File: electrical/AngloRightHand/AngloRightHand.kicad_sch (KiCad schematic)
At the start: 50 parts, among them J4 TC2030-NL, U1 DRV5053VAQDBZR, U10 DRV5053VAQDBZR, U11 DRV5053VAQDBZR, U12 DRV5053VAQDBZR, U13 DRV5053VAQDBZR, U14 DRV5053VAQDBZR, U15 DRV5053VAQDBZR, U16 DRV5053VAQDBZR, U17 DRV5053VAQDBZR, U18 DRV5053VAQDBZR, U19 STM32L072CBTx, U2 CD74HC4067SM, U5 DRV5053VAQDBZR, U6 DRV5053VAQDBZR, U7 DRV5053VAQDBZR, U8 DRV5053VAQDBZR, U9 DRV5053VAQDBZR

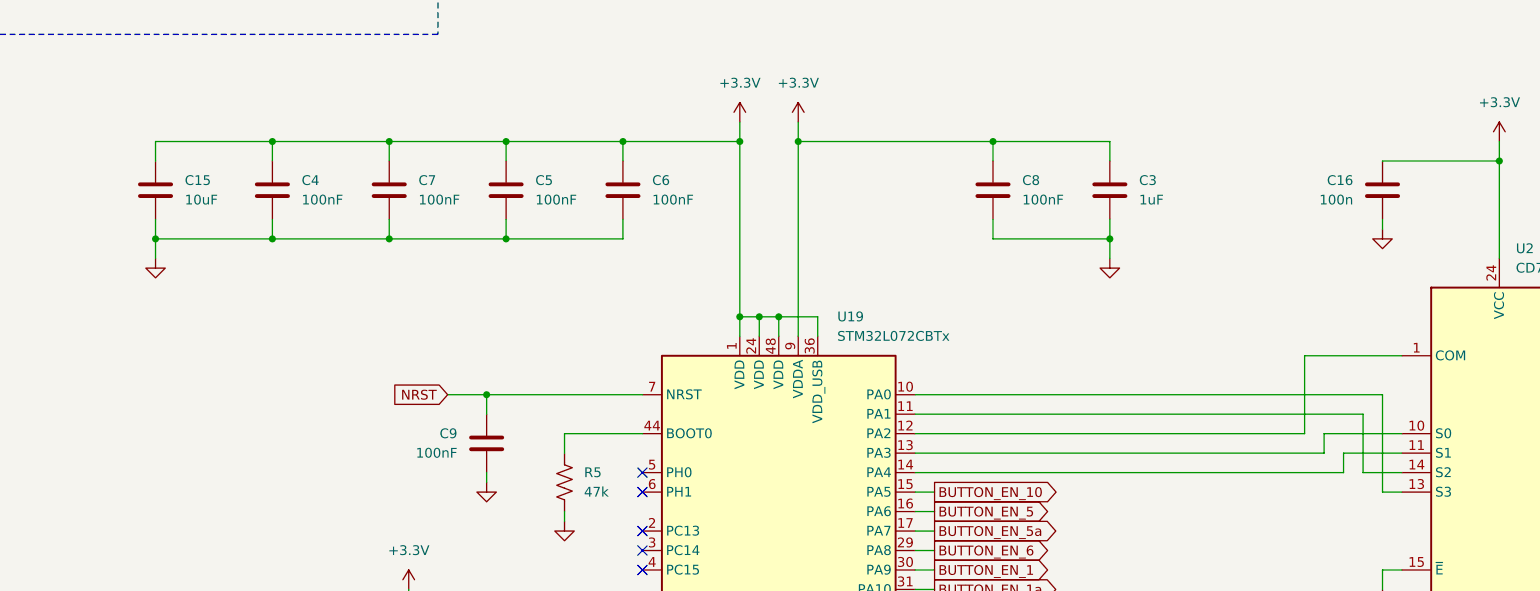
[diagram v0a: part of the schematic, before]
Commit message: All nets routed for right hand board
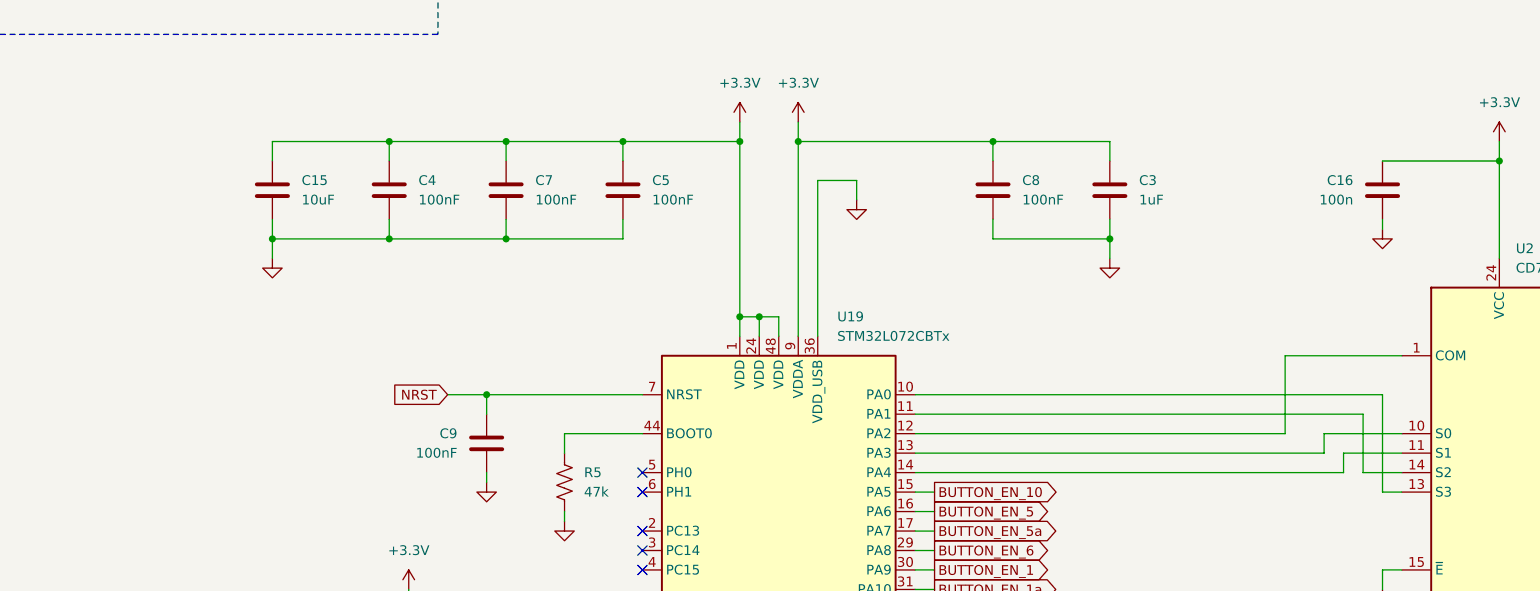
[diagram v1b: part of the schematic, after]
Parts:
- removed C6: 100nF, Capacitor_SMD:C_0402_1005Metric, symbol Device:C
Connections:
- net +3.3V: no longer U19.36 (VDD_USB)
- net GND: now also U19.36 (VDD_USB)
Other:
- moved on the sheet: C15, C4, C5, C7

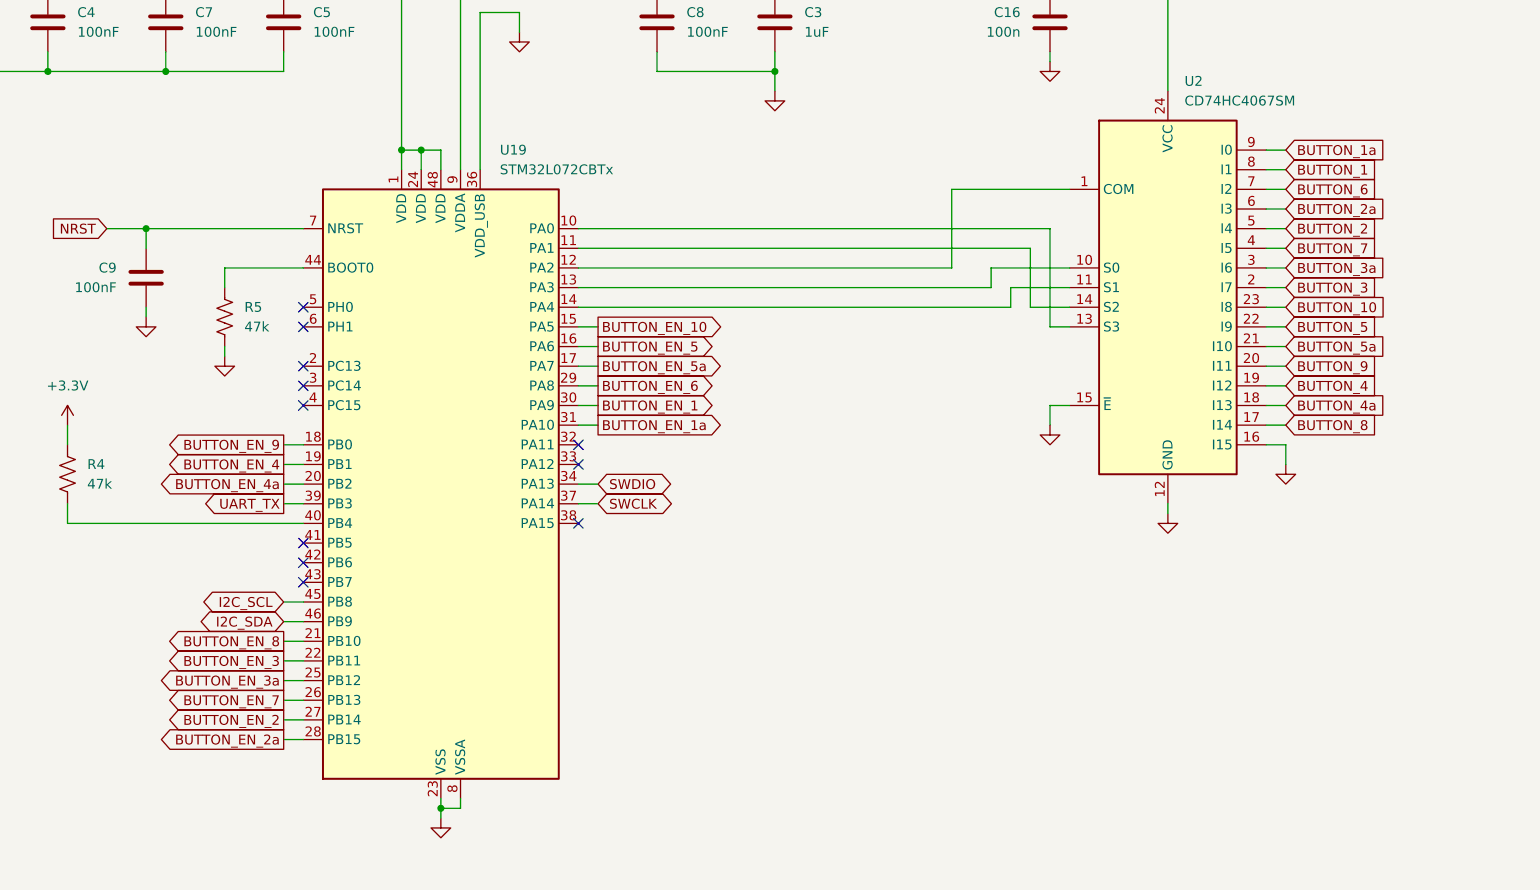
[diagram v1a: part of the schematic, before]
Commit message: Reduce size of right hand board
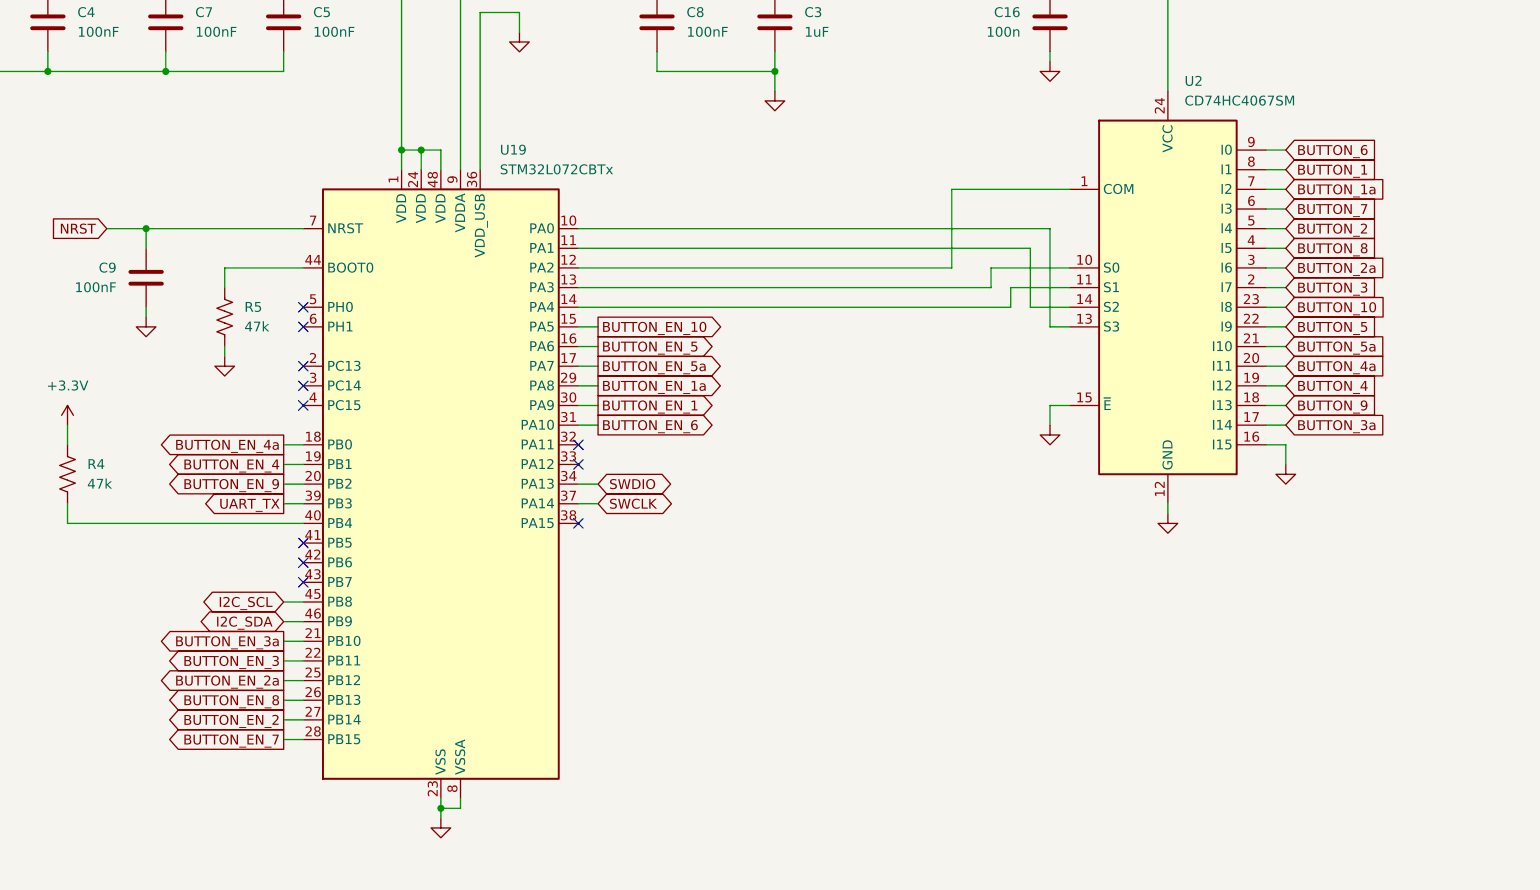
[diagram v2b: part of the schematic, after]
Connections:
- net BUTTON_1a: now also U2.7 (I2); no longer U2.9 (I0)
- net BUTTON_2a: now also U2.3 (I6); no longer U2.6 (I3)
- net BUTTON_3a: now also U2.17 (I14); no longer U2.3 (I6)
- net BUTTON_4a: now also U2.20 (I11); no longer U2.18 (I13)
- net BUTTON_6: now also U2.9 (I0); no longer U2.7 (I2)
- net BUTTON_7: now also U2.6 (I3); no longer U2.4 (I5)
- net BUTTON_8: now also U2.4 (I5); no longer U2.17 (I14)
- net BUTTON_9: now also U2.18 (I13); no longer U2.20 (I11)
- net BUTTON_EN_1a: now also U19.29 (PA8); no longer U19.31 (PA10)
- net BUTTON_EN_2a: now also U19.25 (PB12); no longer U19.28 (PB15)
- net BUTTON_EN_3a: now also U19.21 (PB10); no longer U19.25 (PB12)
- net BUTTON_EN_4a: now also U19.18 (PB0); no longer U19.20 (PB2)
- net BUTTON_EN_6: now also U19.31 (PA10); no longer U19.29 (PA8)
- net BUTTON_EN_7: now also U19.28 (PB15); no longer U19.26 (PB13)
- net BUTTON_EN_8: now also U19.26 (PB13); no longer U19.21 (PB10)
- net BUTTON_EN_9: now also U19.20 (PB2); no longer U19.18 (PB0)

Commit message: Clean up right hand schematic
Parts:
- renumbered C15 to C1, C21 to C10, C20 to C11, C22 to C12, C23 to C13, C24 to C14, C25 to C15, C26 to C16, C27 to C17, C28 to C18, C29 to C19, C4 to C2, C30 to C20, C31 to C21, C32 to C22, C33 to C23, C34 to C24, C35 to C25, C7 to C3, C5 to C4, C8 to C5, C3 to C6, C16 to C7, C9 to C8, C19 to C9, J5 to J1, J6 to J2, J4 to J3, R5 to R1, R4 to R2, U19 to U1, U11 to U10, U12 to U11, U13 to U12, U14 to U13, U15 to U14, U16 to U15, U17 to U16, U18 to U17, U1 to U3, U5 to U4, U6 to U5, U7 to U6, U8 to U7, U9 to U8, U10 to U9
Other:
- note removed: "Hardware"
- moved on the sheet: C1, C10, C11, C12, C13, C14, C15, C16, C17, C18, C19, C2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

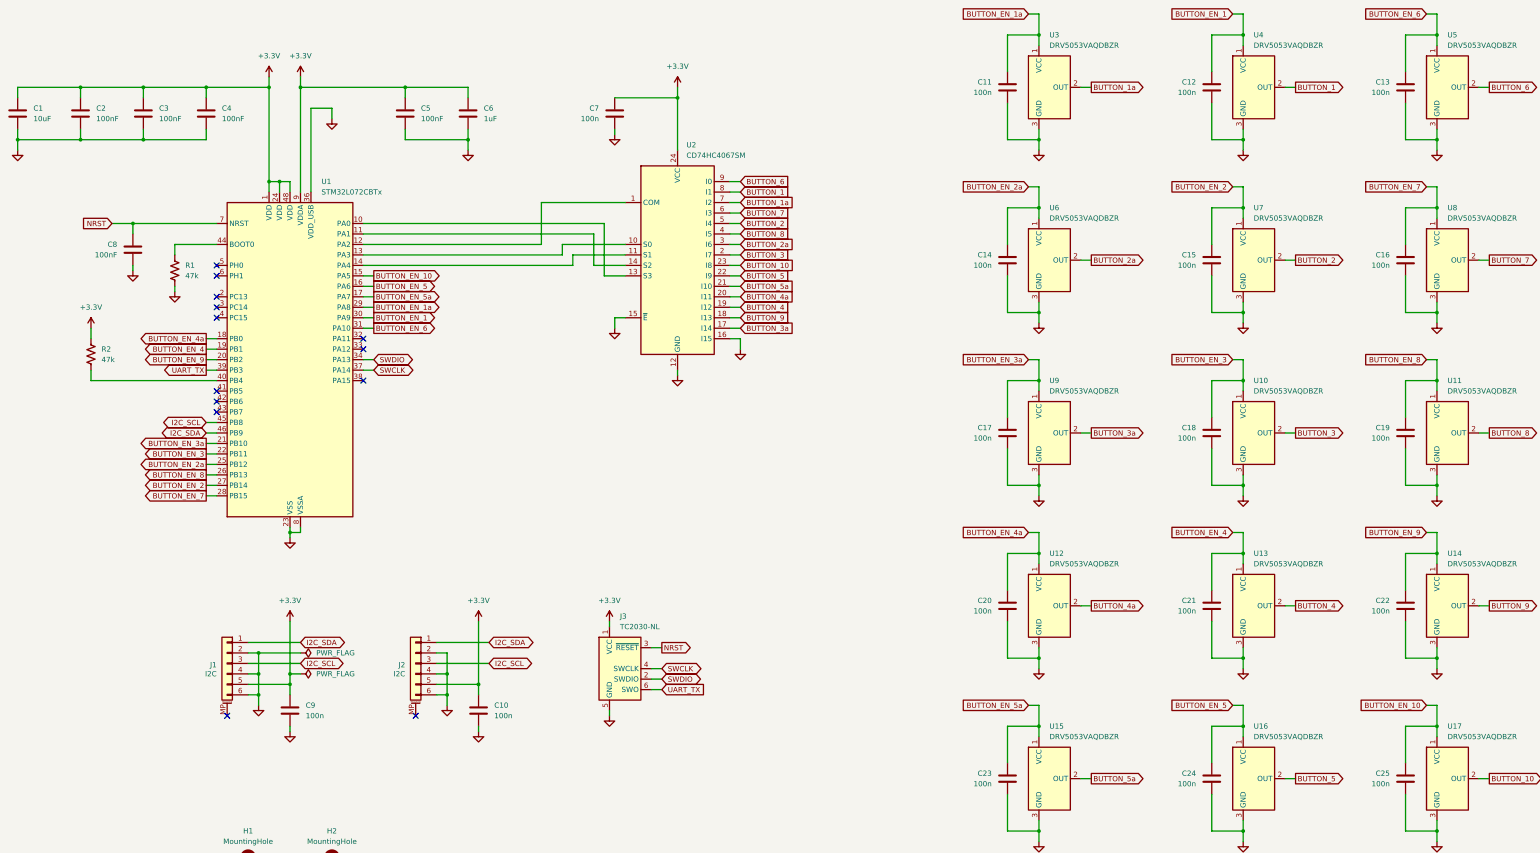
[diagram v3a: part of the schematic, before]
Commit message: Renumber parts on right hand board
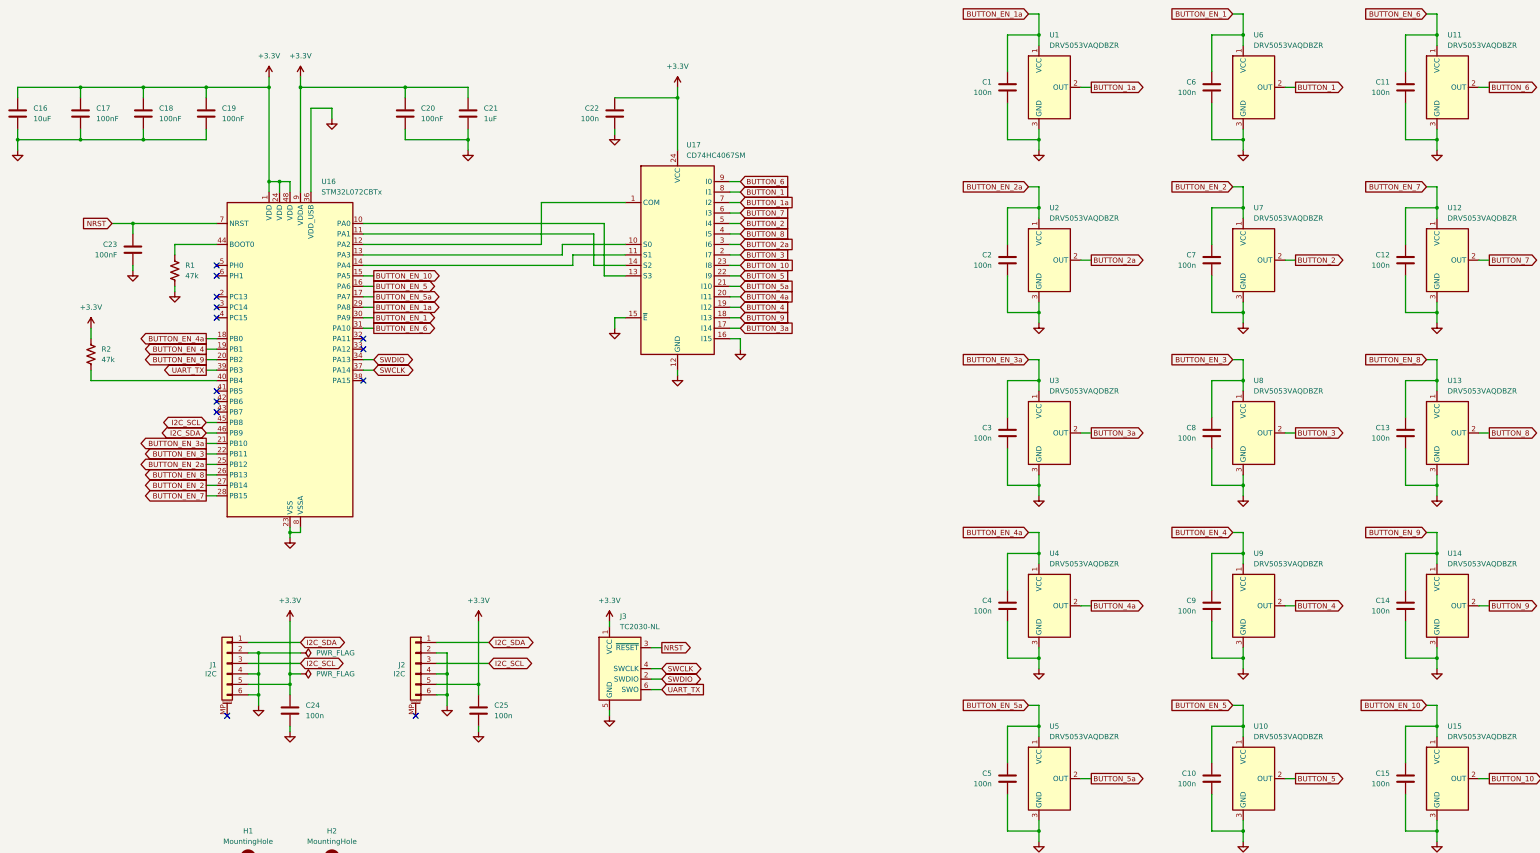
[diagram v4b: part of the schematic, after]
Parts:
- renumbered C11 to C1, C24 to C10, C13 to C11, C16 to C12, C19 to C13, C22 to C14, C25 to C15, C1 to C16, C2 to C17, C3 to C18, C4 to C19, C14 to C2, C5 to C20, C6 to C21, C7 to C22, C8 to C23, C9 to C24, C10 to C25, C17 to C3, C20 to C4, C23 to C5, C12 to C6, C15 to C7, C18 to C8, C21 to C9, U3 to U1, U16 to U10, U5 to U11, U8 to U12, U11 to U13, U17 to U15, U1 to U16, U2 to U17, U6 to U2, U9 to U3, U12 to U4, U15 to U5, U4 to U6, U10 to U8, U13 to U9

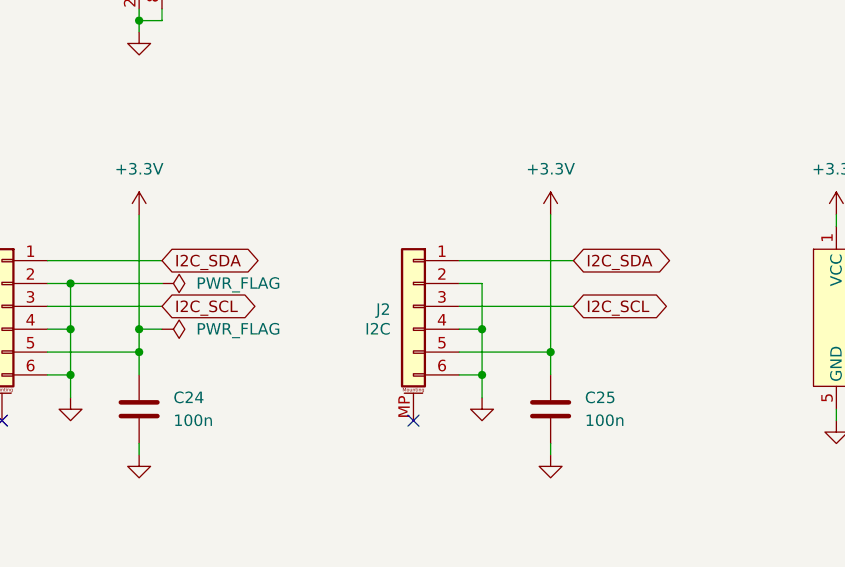
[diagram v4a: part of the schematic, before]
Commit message: Swap SDA and SCL on button board connectors
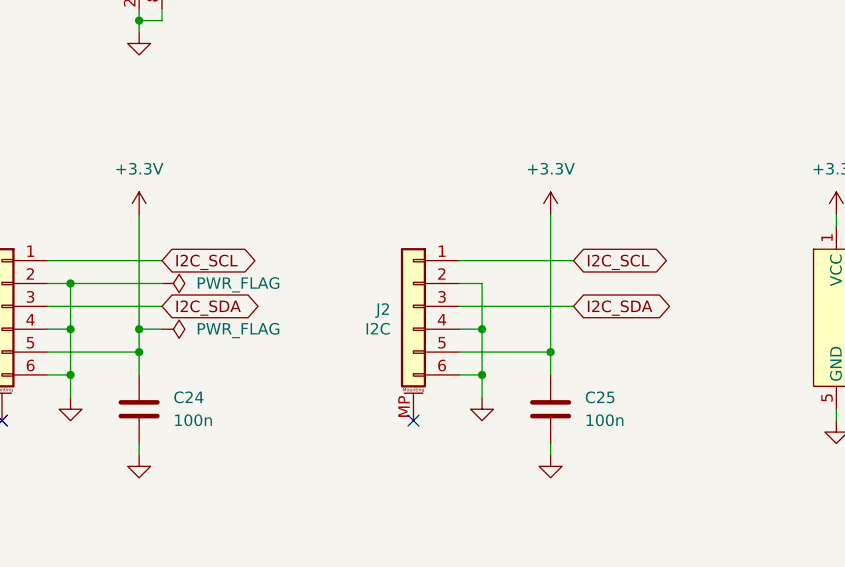
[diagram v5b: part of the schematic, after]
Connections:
- net I2C_SCL: now also J1.1 (Pin_1), J2.1 (Pin_1); no longer J1.3 (Pin_3), J2.3 (Pin_3)
- net I2C_SDA: now also J1.3 (Pin_3), J2.3 (Pin_3); no longer J1.1 (Pin_1), J2.1 (Pin_1)
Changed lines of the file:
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@@
 	(global_label "I2C_SDA"
 		(shape bidirectional)
-		(at 109.22 176.53 0)
-		(fields_autoplaced yes)
-		(effects
-			(font
-				(size 1.27 1.27)
-			)
-			(justify left)
-		)
-		(property "Intersheetrefs" "${INTERSHEET_REFS}"
-			(at 120.9365 176.53 0)
+		(at 109.22 181.61 0)
+		(fields_autoplaced yes)
+		(effects
+			(font
+				(size 1.27 1.27)
+			)
+			(justify left)
+		)
+		(property "Intersheetrefs" "${INTERSHEET_REFS}"
+			(at 120.9365 181.61 0)
 			(effects
 				(font
@@
 	(global_label "I2C_SCL"
 		(shape bidirectional)
-		(at 109.22 181.61 0)
-		(fields_autoplaced yes)
-		(effects
-			(font
-				(size 1.27 1.27)
-			)
-			(justify left)
-		)
-		(property "Intersheetrefs" "${INTERSHEET_REFS}"
-			(at 120.876 181.61 0)
+		(at 109.22 176.53 0)
+		(fields_autoplaced yes)
+		(effects
+			(font
+				(size 1.27 1.27)
+			)
+			(justify left)
+		)
+		(property "Intersheetrefs" "${INTERSHEET_REFS}"
+			(at 120.876 176.53 0)
 			(effects
 				(font
@@
 	(global_label "I2C_SDA"
 		(shape bidirectional)
-		(at 154.94 176.53 0)
-		(fields_autoplaced yes)
-		(effects
-			(font
-				(size 1.27 1.27)
-			)
-			(justify left)
-		)
-		(property "Intersheetrefs" "${INTERSHEET_REFS}"
-			(at 166.6565 176.53 0)
+		(at 154.94 181.61 0)
+		(fields_autoplaced yes)
+		(effects
+			(font
+				(size 1.27 1.27)
+			)
+			(justify left)
+		)
+		(property "Intersheetrefs" "${INTERSHEET_REFS}"
+			(at 166.6565 181.61 0)
 			(effects
 				(font
@@
 	(global_label "I2C_SCL"
 		(shape bidirectional)
-		(at 154.94 181.61 0)
-		(fields_autoplaced yes)
-		(effects
-			(font
-				(size 1.27 1.27)
-			)
-			(justify left)
-		)
-		(property "Intersheetrefs" "${INTERSHEET_REFS}"
-			(at 166.596 181.61 0)
-			(effects
-				(font
+		(at 154.94 176.53 0)
+		(fields_autoplaced yes)
+		(effects
+			(font
+				(size 1.27 1.27)
+			)
+			(justify left)
+		)
+		(property "Intersheetrefs" "${INTERSHEET_REFS}"
+			(at 166.596 176.53 0)
+			(effects
+				(font
